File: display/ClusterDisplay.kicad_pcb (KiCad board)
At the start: 6 copper layers, 178.2 x 105 mm, 172 parts, among them J1 Verdin iMX95 Hexa 8GB WB IT, J10 RTC coin cell, J11 Molex KK-254 22-27-2041, rota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, J12 Samtec TSW-103-07-G-S A55 con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, J13 Samtec TSW-105-07-G-S USB_1 O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, J14 JST XH B5B-XH-A balanced line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, J15 JST XH B3B-XH-A electret micr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, J16 MFi daughterboard header I2C_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, J17 GCT USB4105-GF-A USB-C 2.0 ho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, J2 Phoenix MKDS 1,5/3-5,08 power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, J3 Molex KK-254 22-27-2031 priva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, J4 TST040HDBC-42 panel, J8 Samtec TSW-108-07-G-S JTAG (b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, J9 Samtec TSW-104-07-G-S buttons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, Q1 SQJ460AEP (AEC-Q101, 60V/20V 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, Q2 SQJ460AEP (AEC-Q101, 60V/20V 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, Q3 PMV55ENEA ignition wake pulld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, U1 LM74930-Q1, U10 TLV767-Q1 (3.3 V audio AVDD), U11 TPS2557-Q1, U12 TPD4E02B04-Q1 line-out ESD (b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, U13 TPD4E05U06-Q1 mic ESD, U14 TPD4E05U06-Q1 USB ESD, U15 TPS22918-Q1 (AEC-Q100 G2) MFi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, U2 LM61460-Q1, U3 TLV767-Q1, U4 TCAN1044V-Q1, U6 TPS65131-Q1, U7 TPS61165-Q1, U8 TPS22918-Q1 (AEC-Q100 G2) dia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, U9 TAC5112-Q1

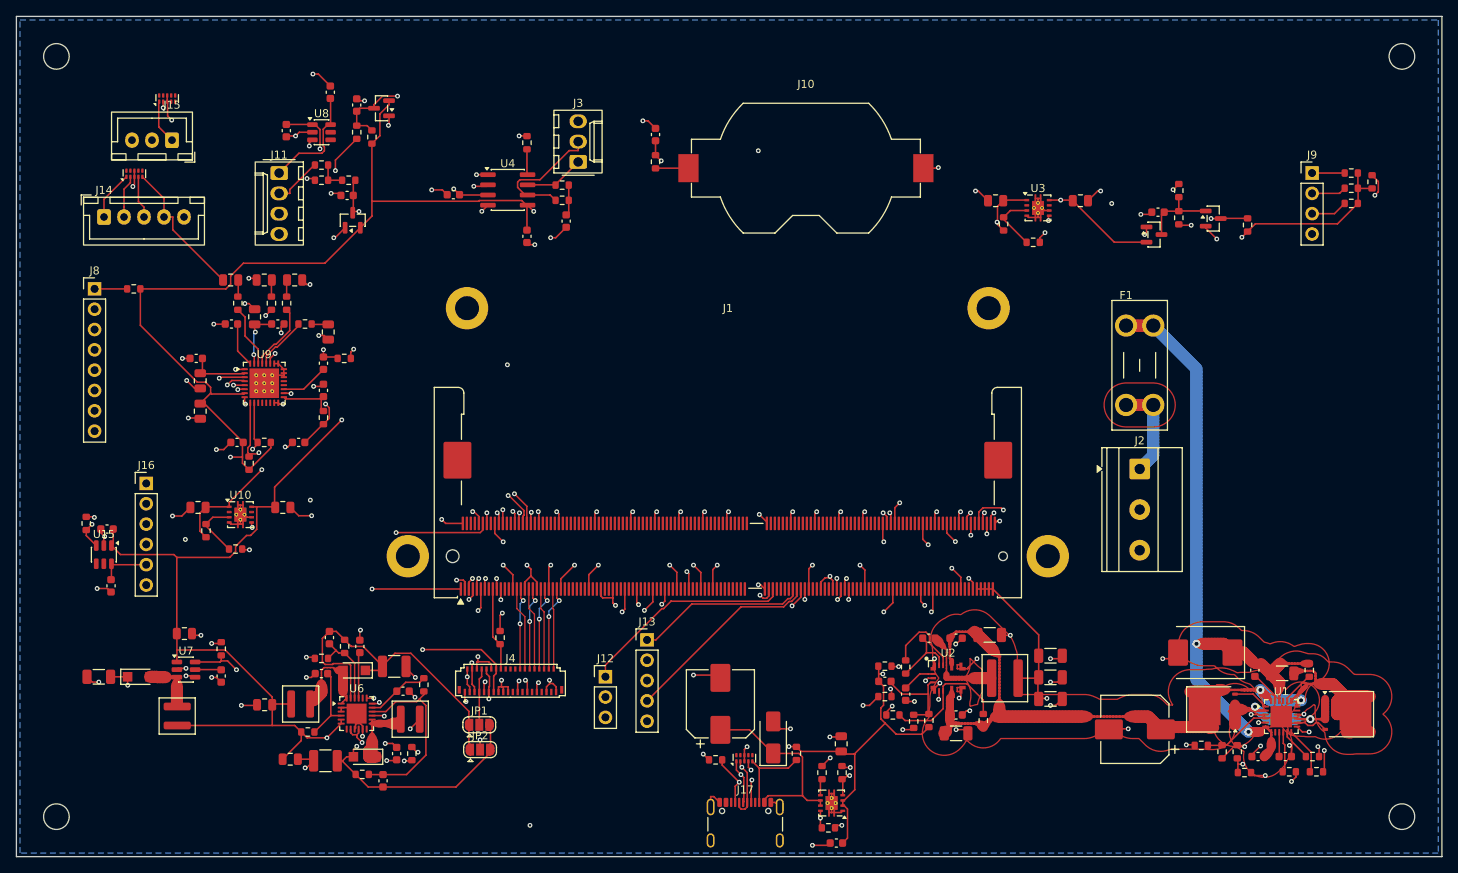
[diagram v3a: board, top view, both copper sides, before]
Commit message: Move R2 and C3 off the display battery path's R1 -> Q2 line
The first battery-path route threaded SENSE_OUT (2.6 A) between R2's own
0603 pads at 0.3 mm. display/cells.py now pulls R2's VBAT_F end to R1's
input pad (the Kelvin point RSET wants) and C3's to U1's VS pin, and
places C3 before R2, so both sit on R1's input side. Re-routed: SENSE_OUT
passes the 20 K check (worst 2 K); COMMON and +12V_PROT keep only pin
necks of 7 mW or less. 0 unconnected, accepted DRC only, fab gate passes.

display-rgb/ keeps its first route: it is to be replaced with display/
by a generic brain board, so it was not re-placed.

Co-Authored-By: Claude Opus 5.5 <noreply@anthropic.com>
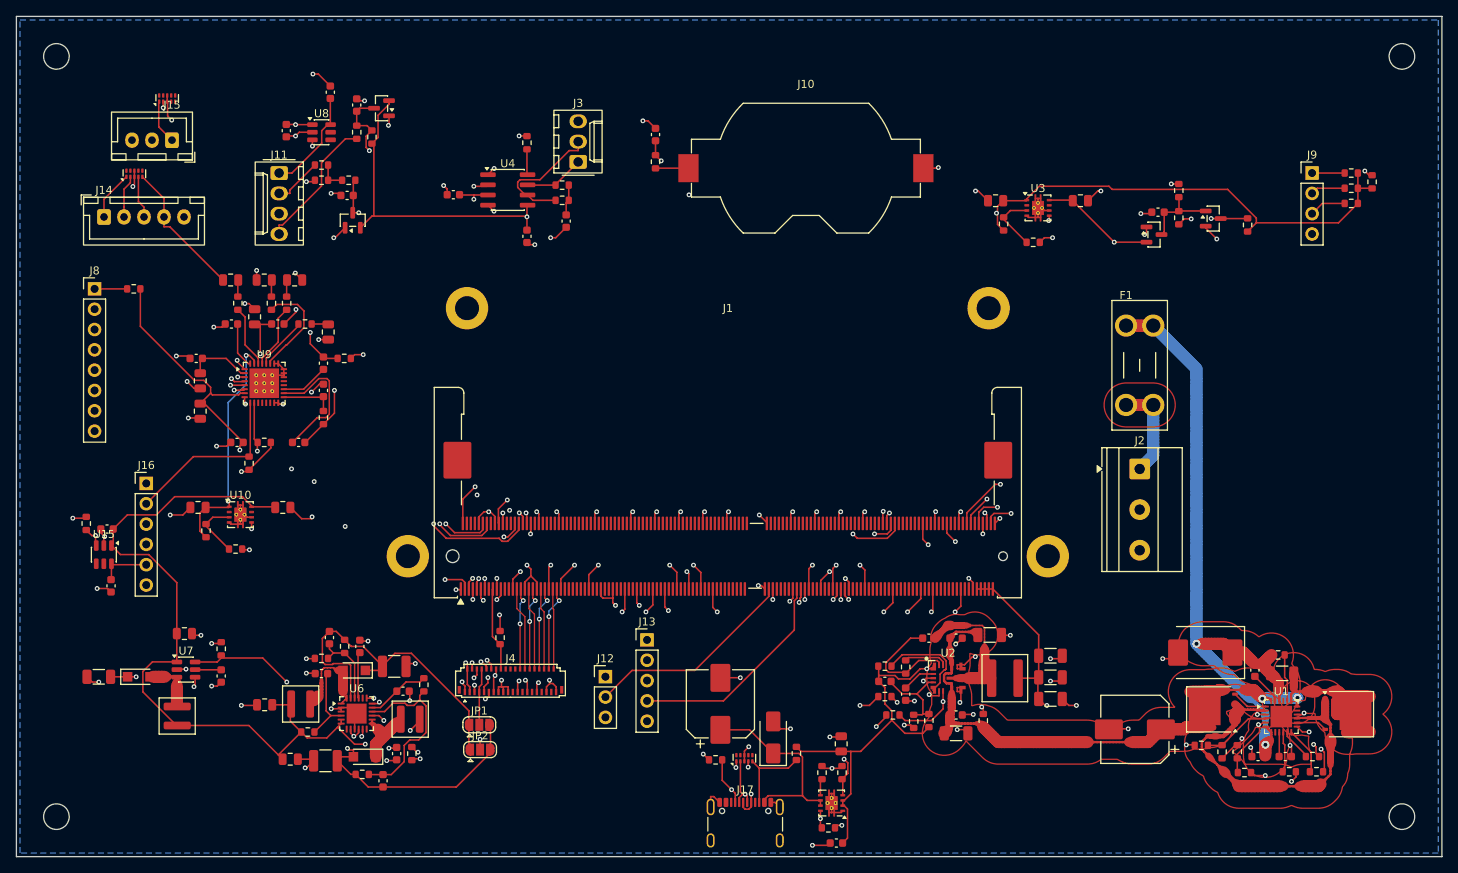
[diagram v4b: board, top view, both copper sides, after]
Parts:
- moved R2 4.34 mm to (278.6, 175.8), turned to 0 degrees
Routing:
- net +5V: track 447.3 -> 481.3 mm, vias 11 -> 8
- net COMMON: track 20.4 -> 44.2 mm, vias 2 -> 0
- net IGN_SENSE: track 53.4 -> 72.1 mm
- net RESET_MICO: track 197.6 -> 179.8 mm
- net RECOVERY: track 82.1 -> 65.4 mm
- net RESET_MOCI: track 82.6 -> 67.7 mm, vias 3 -> 2
- net I2S_BCLK: track 60.4 -> 46.3 mm, vias 3 -> 2
- net PWR_BTN: track 88.7 -> 75.6 mm
- net I2C1_SCL: track 58.1 -> 67.5 mm, vias 2 -> 1
- net DIAL_CLICK: track 93.9 -> 103.1 mm, vias 2 -> 3
- net MIC_IN_P: track 9.03 -> 16.8 mm, vias 2 -> 0
- net +12V_PROT: track 81.1 -> 73.4 mm
- net SW_5V: track 11.3 -> 17.7 mm
- net BOOT_C: track 8.55 -> 14.7 mm
- net JTAG_TDI: track 57.2 -> 62.8 mm
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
